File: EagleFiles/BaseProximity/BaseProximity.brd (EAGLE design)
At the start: 80 x 60 mm, 26 parts, among them Q1 2N3904, Q3 2N3904

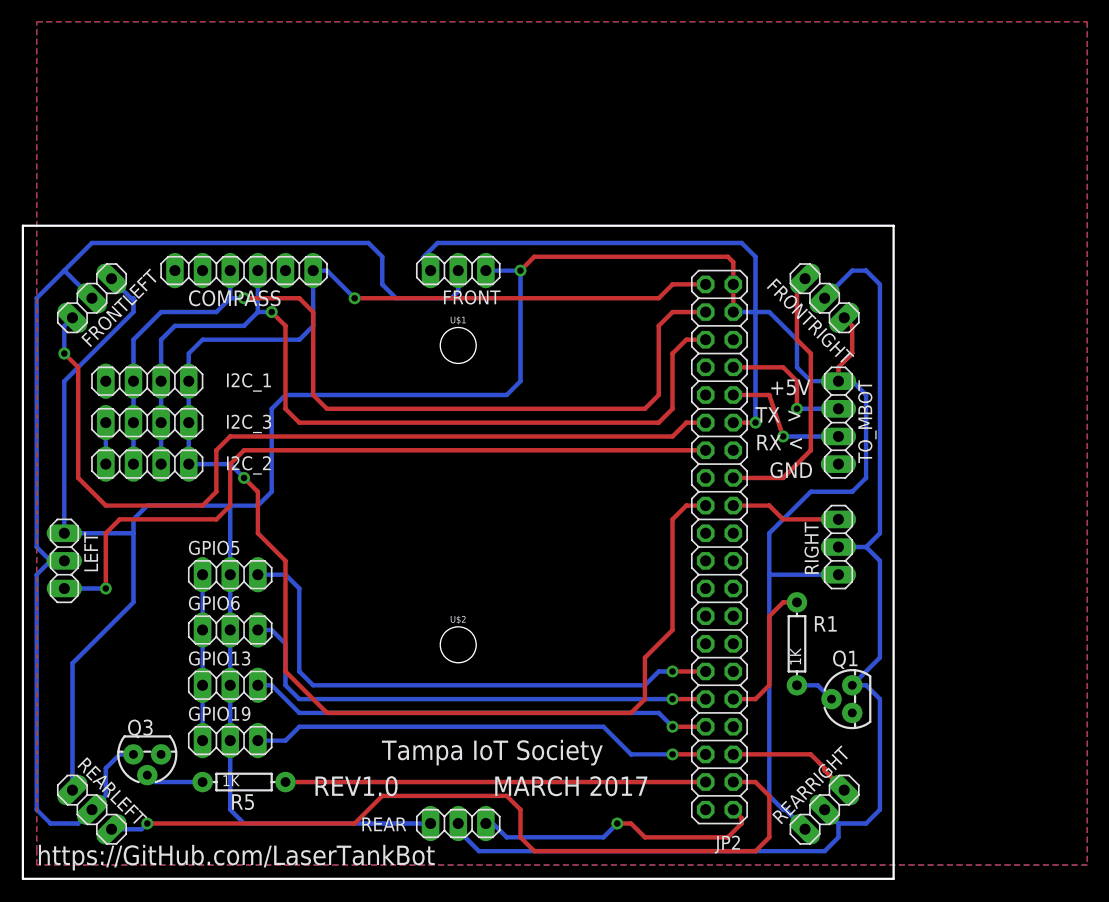
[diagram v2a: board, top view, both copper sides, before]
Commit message: updated board for new order
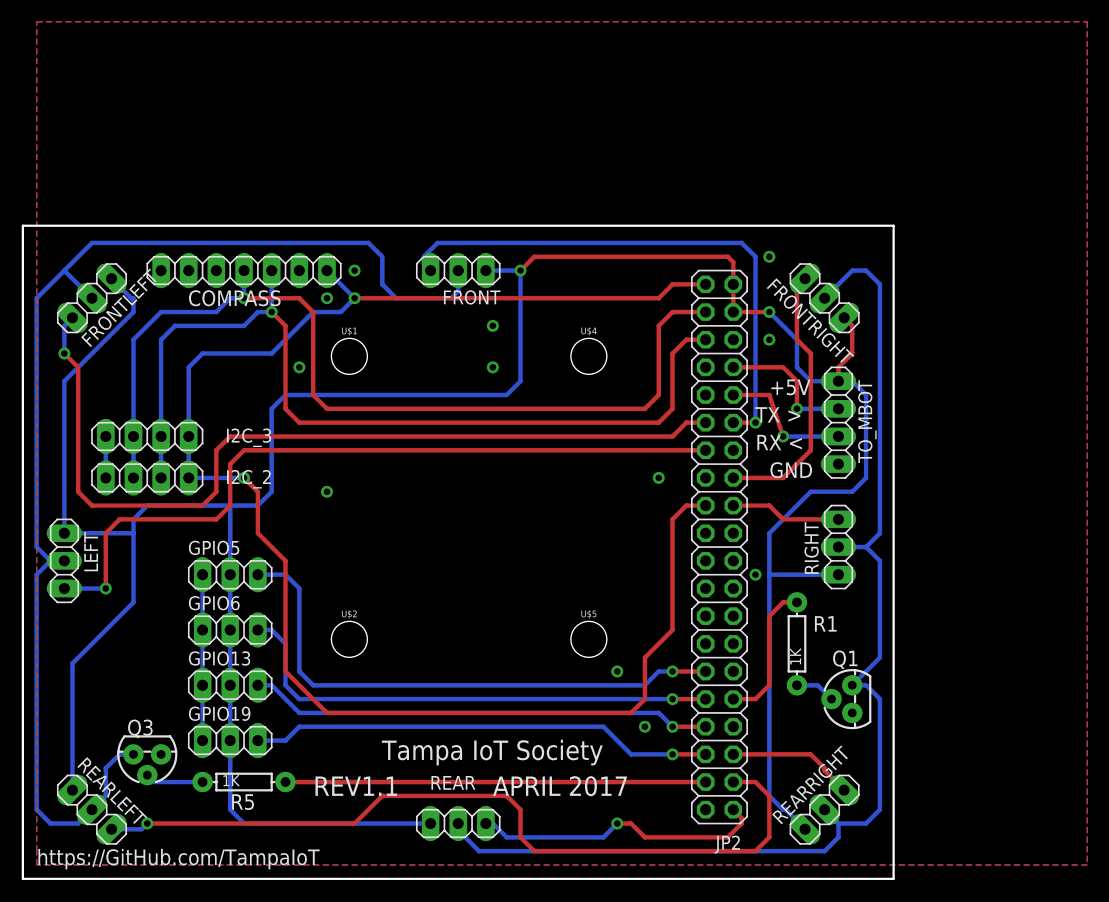
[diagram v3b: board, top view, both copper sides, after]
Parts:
- removed I2C_1: (no value), pinhead:1X04
- added U$4, U$5: (no value), SparkFun-Hardware:STAND-OFF
- COMPASS: device pinhead:1X06 -> pinhead:1X07
- moved U$1 10.0 mm to (30.0, 48.0)
- moved U$2 10.0 mm to (30.0, 22.0)
- moved I2C_2 1.27 mm to (11.4, 36.8)
- moved I2C_3 1.27 mm to (11.4, 40.6)
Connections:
- new net N$5: COMPASS.3
- net GND: now also COMPASS.6; no longer COMPASS.5, I2C_1.4
- net SCL: now also COMPASS.5; no longer COMPASS.4, I2C_1.2
- net SDA: now also COMPASS.4; no longer COMPASS.3, I2C_1.3
- net VCC: now also COMPASS.7; no longer COMPASS.6, I2C_1.1
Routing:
- net VCC: track 146.6 -> 145.1 mm
- net SDA: track 84.2 -> 85.5 mm
- net SCL: track 81.1 -> 82.4 mm
- net GPIO17: track 79.6 -> 80.4 mm
- net GND: track 19.0 -> 19.1 mm, vias 0 -> 12
- net +5V: vias 1 -> 2
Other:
- board text added: "APRIL 2017"
- board text added: "REV1.1"
- board text added: "https://GitHub.com/TampaIoT"
- board text removed: "MARCH 2017"
- board text removed: "REV1.0"
- board text removed: "https://GitHub.com/LaserTankBot"
